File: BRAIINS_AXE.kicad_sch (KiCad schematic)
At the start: 5 parts, among them J9 molex_mini_fit

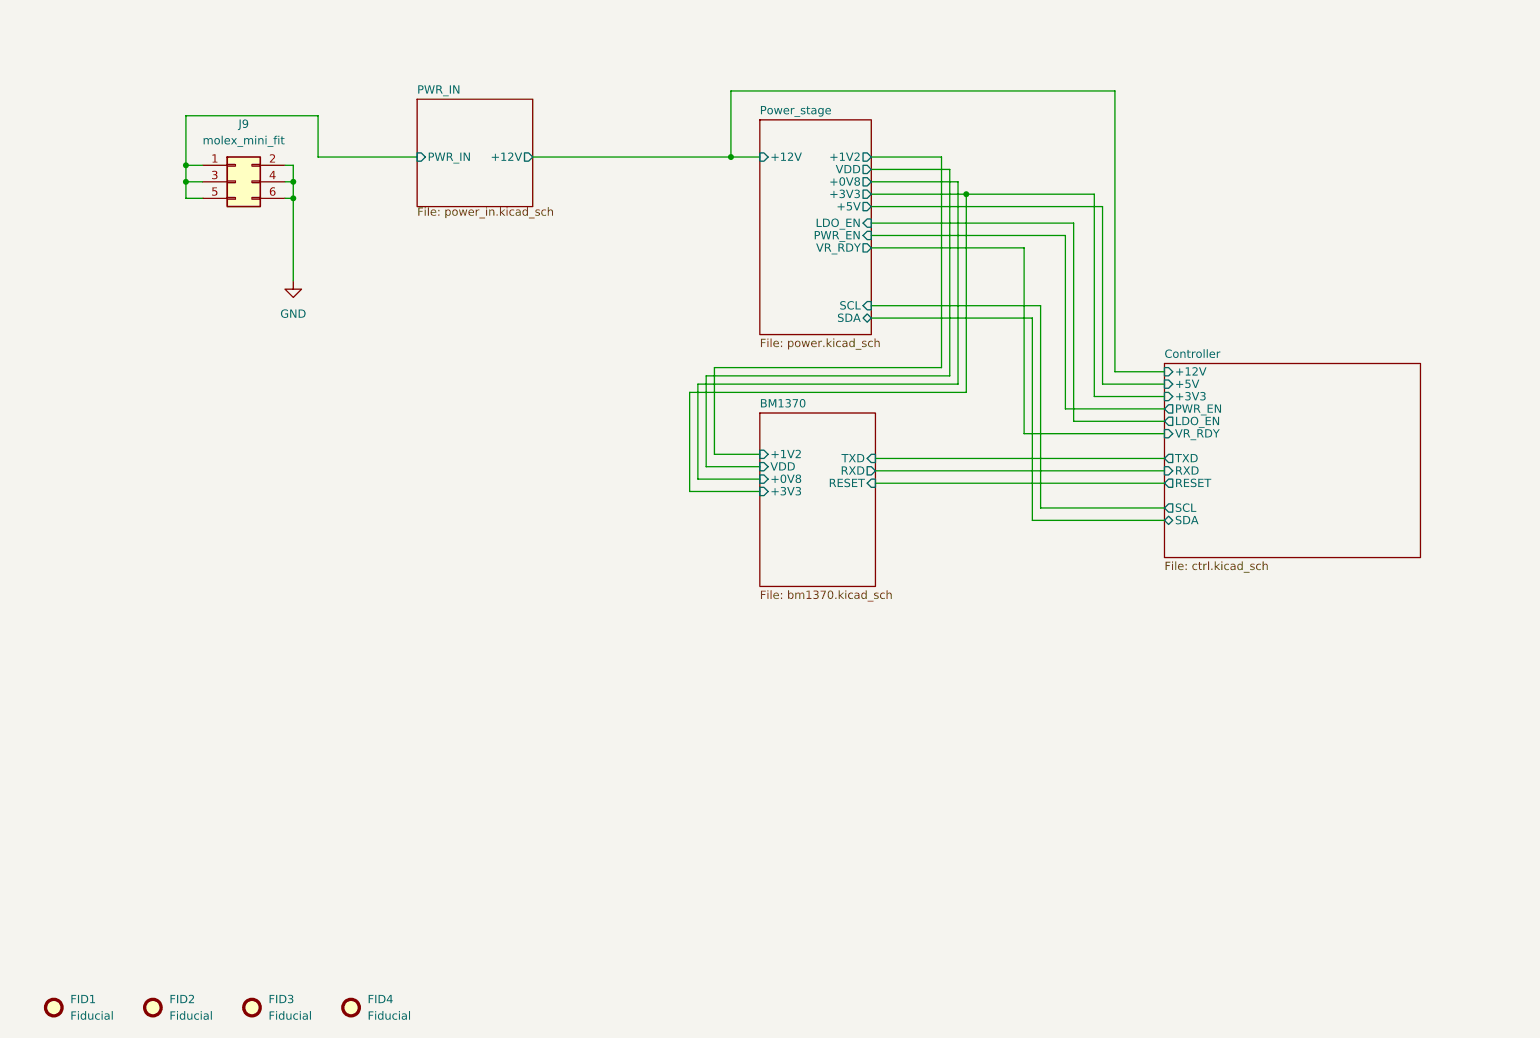
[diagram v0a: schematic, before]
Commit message: updated power stage placements
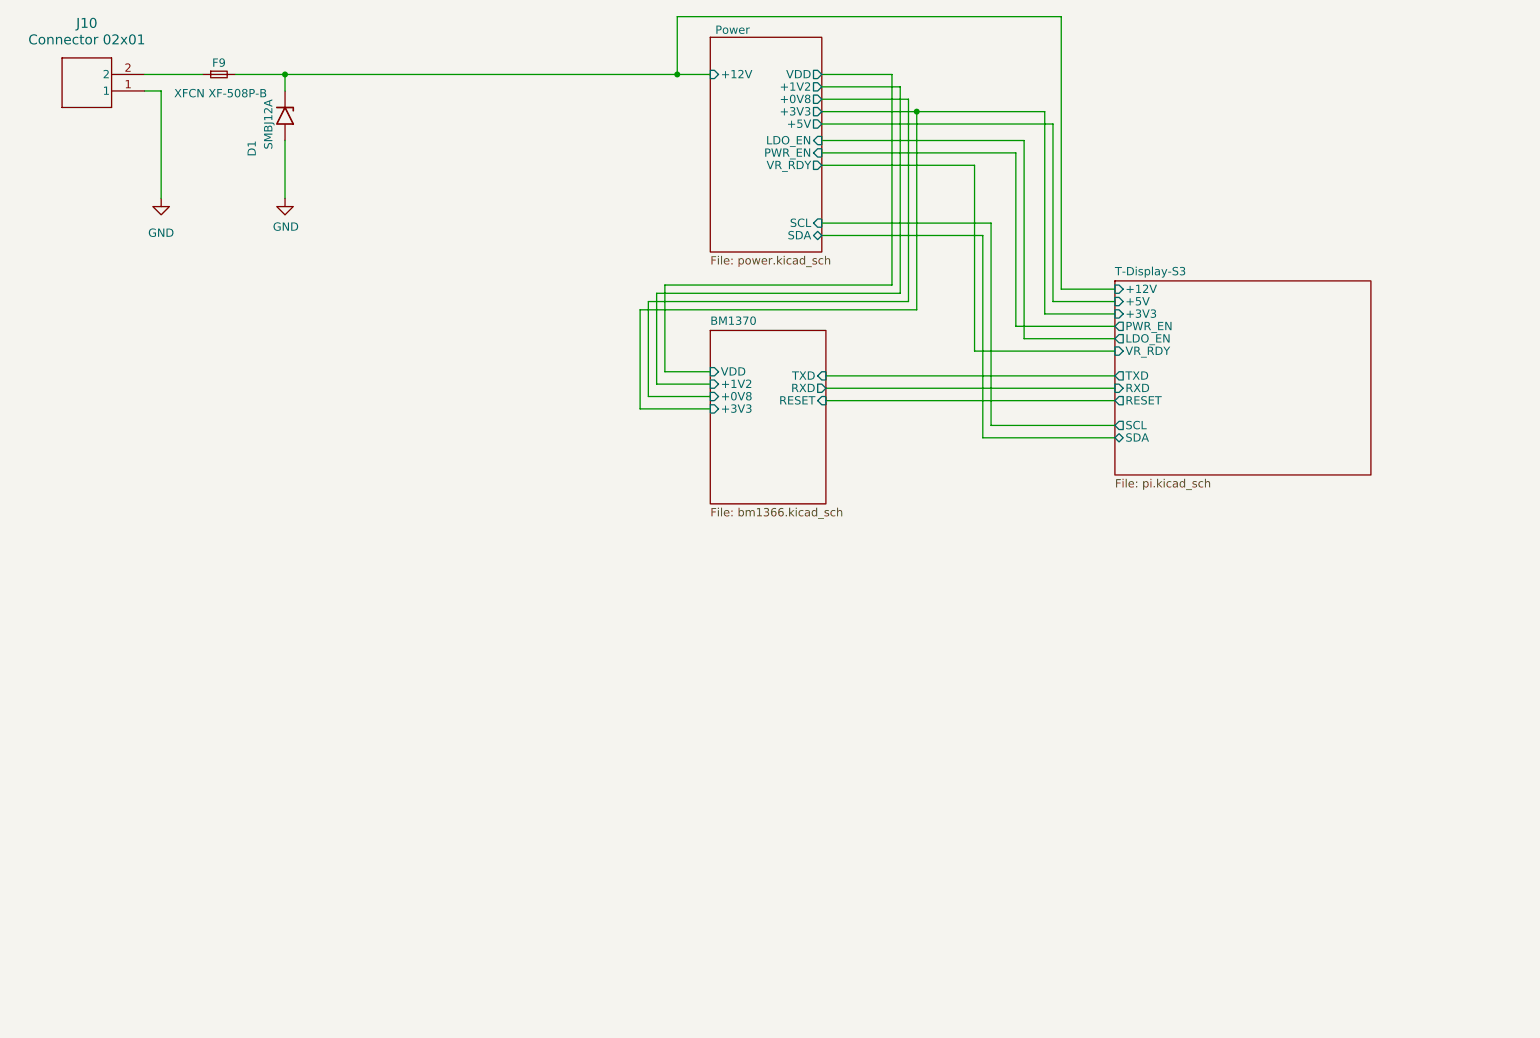
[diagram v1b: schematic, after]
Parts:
- removed FID1, FID2, FID3, FID4: Fiducial, Fiducial:Fiducial_1mm_Mask2mm, symbol Mechanical:Fiducial
- removed J9: molex_mini_fit, Connector_Molex:Molex_Mini-Fit_Jr_5569-06A2_2x03_P4.20mm_Horizontal, symbol Connector_Generic:Conn_02x03_Odd_Even
- added D1: SMBJ12A, Diode_SMD:D_SMB, symbol Diode:5KPxxA
- added F9: XFCN XF-508P-B, Nerd8:XFCN XF-508P-B, symbol Device:Fuse_Small
- added J10: Connector 02x01, Connector_AMASS:AMASS_XT60PW-M_1x02_P7.20mm_Horizontal, symbol CONN02:OSTYK51102030
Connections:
- net GND: now also D1.2 (A2), J10.1
- new net: F9.1, J10.2
- new net Power/+12V: D1.1 (A1), F9.2
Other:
- sheet Controller renamed T-Display-S3
- sheet Power_stage renamed Power
- removed sheet PWR_IN
- sheet BM1370: file bm1370.kicad_sch -> bm1366.kicad_sch
- sheet T-Display-S3: file ctrl.kicad_sch -> pi.kicad_sch

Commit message: power stage in place
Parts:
- added H1, H2: MountingHole, MountingHole:MountingHole_3.2mm_M3_Pad_Via, symbol Mechanical:MountingHole
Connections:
- net Power/+12V: no longer D1.1 (A1)
- net at F9.1, J10.2: now also D1.1 (A1)
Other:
- sheet T-Display-S3 renamed controller
- sheet controller: file pi.kicad_sch -> CONTROL.kicad_sch
- moved on the sheet: D1, F9
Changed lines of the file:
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@@
 	)
 	(junction
-		(at 55.88 52.07)
+		(at 46.99 52.07)
 		(diameter 0)
 		(color 0 0 0 0)
@@
 	(wire
 		(pts
+			(xy 46.99 52.07) (xy 55.88 52.07)
+		)
+		(stroke
+			(width 0)
+			(type default)
+		)
+	)
+	(wire
+		(pts
 			(xy 138.43 76.835) (xy 163.195 76.835)
 		)
@@
 	(wire
 		(pts
-			(xy 34.29 52.07) (xy 43.18 52.07)
+			(xy 34.29 52.07) (xy 46.99 52.07)
 		)
 		(stroke
@@
 	(wire
 		(pts
-			(xy 48.26 52.07) (xy 55.88 52.07)
-		)
-		(stroke
-			(width 0)
-			(type default)
-		)
-	)
-	(wire
-		(pts
 			(xy 149.225 52.07) (xy 149.225 84.455)
 		)
@@
 	(wire
 		(pts
-			(xy 55.88 54.61) (xy 55.88 52.07)
+			(xy 46.99 54.61) (xy 46.99 52.07)
 		)
 		(stroke
@@
 	(wire
 		(pts
+			(xy 60.96 52.07) (xy 116.205 52.07)
+		)
+		(stroke
+			(width 0)
+			(type default)
+		)
+	)
+	(wire
+		(pts
 			(xy 138.43 66.04) (xy 161.925 66.04)
 		)
@@
 	(wire
 		(pts
-			(xy 55.88 62.23) (xy 55.88 71.12)
+			(xy 46.99 62.23) (xy 46.99 71.12)
 		)
 		(stroke
@@
 		(pts
 			(xy 161.925 66.04) (xy 161.925 94.615)
-		)
-		(stroke
-			(width 0)
-			(type default)
-		)
-	)
-	(wire
-		(pts
-			(xy 55.88 52.07) (xy 116.205 52.07)
 		)
 		(stroke
@@
 	(symbol
 		(lib_id "power:GND")
-		(at 55.88 71.12 0)
+		(at 46.99 71.12 0)
 		(unit 1)
 		(body_style 1)
@@
 		(dnp no)
 		(property "Reference" "#PWR04"
-			(at 55.88 77.47 0)
+			(at 46.99 77.47 0)
 			(hide yes)
 			(show_name no)
@@
 		)
 		(property "Value" "GND"
-			(at 56.007 75.5142 0)
+			(at 47.117 75.5142 0)
 			(show_name no)
 			(do_not_autoplace no)
@@
 		)
 		(property "Footprint" ""
-			(at 55.88 71.12 0)
+			(at 46.99 71.12 0)
 			(hide yes)
 			(show_name no)
@@
 		)
 		(property "Datasheet" ""
-			(at 55.88 71.12 0)
+			(at 46.99 71.12 0)
 			(hide yes)
 			(show_name no)
@@
 		)
 		(property "Description" ""
-			(at 55.88 71.12 0)
+			(at 46.99 71.12 0)
 			(hide yes)
 			(show_name no)
@@
 	(symbol
 		(lib_id "Diode:5KPxxA")
-		(at 55.88 58.42 270)
+		(at 46.99 58.42 270)
 		(unit 1)
 		(body_style 1)
@@
 		(dnp no)
 		(property "Reference" "D1"
-			(at 50.8 62.23 0)
+			(at 48.26 61.722 90)
 			(show_name no)
 			(do_not_autoplace no)
@@
 		)
 		(property "Value" "SMBJ12A"
-			(at 53.34 55.88 0)
+			(at 44.45 55.88 0)
 			(show_name no)
 			(do_not_autoplace no)
@@
 		)
 		(property "Footprint" "Diode_SMD:D_SMB"
-			(at 50.8 58.42 0)
+			(at 41.91 58.42 0)
 			(hide yes)
 			(show_name no)
@@
 		)
 		(property "Datasheet" ""
-			(at 55.88 57.15 0)
+			(at 46.99 57.15 0)
 			(hide yes)
 			(show_name no)
@@
 		)
 		(property "Description" "TVS DIODE 12VWM 19.9VC DO214AA"
-			(at 55.88 58.42 0)
+			(at 46.99 58.42 0)
 			(hide yes)
 			(show_name no)
@@
 		)
 		(property "Distributor" "D"
-			(at 55.88 58.42 0)
+			(at 46.99 58.42 0)
 			(hide yes)
 			(show_name no)
@@
 		)
 		(property "Manufacturer" "SMBJ12A"
-			(at 55.88 58.42 0)
+			(at 46.99 58.42 0)
 			(hide yes)
 			(show_name no)
@@
 		)
 		(property "OrderNr" "SMBJ12ALFCT-ND"
-			(at 55.88 58.42 0)
+			(at 46.99 58.42 0)
 			(hide yes)
 			(show_name no)
@@
 	)
 	(symbol
+		(lib_id "Mechanical:MountingHole")
+		(at 165.1 161.29 0)
+		(unit 1)
+		(body_style 1)
+		(exclude_from_sim no)
+		(in_bom no)
+		(on_board yes)
+		(in_pos_files yes)
+		(dnp no)
+		(fields_autoplaced yes)
+		(property "Reference" "H1"
+			(at 167.64 160.0199 0)
+			(show_name no)
+			(do_not_autoplace no)
+			(effects
+				(font
+					(size 1.27 1.27)
+				)
+				(justify left)
+			)
+		)
+		(property "Value" "MountingHole"
+			(at 167.64 162.5599 0)
+			(show_name no)
+			(do_not_autoplace no)
+			(effects
+				(font
+					(size 1.27 1.27)
+				)
+				(justify left)
+			)
+		)
+		(property "Footprint" "MountingHole:MountingHole_3.2mm_M3_Pad_Via"
+			(at 165.1 161.29 0)
+			(hide yes)
+			(show_name no)
+			(do_not_autoplace no)
+			(effects
+				(font
+					(size 1.27 1.27)
+				)
+			)
+		)
+		(property "Datasheet" ""
+			(at 165.1 161.29 0)
+			(hide yes)
+			(show_name no)
+			(do_not_autoplace no)
+			(effects
+				(font
+					(size 1.27 1.27)
+				)
+			)
+		)
+		(property "Description" "Mounting Hole without connection"
+			(at 165.1 161.29 0)
+			(hide yes)
+			(show_name no)
+			(do_not_autoplace no)
+			(effects
+				(font
+					(size 1.27 1.27)
+				)
+			)
+		)
+		(instances
+			(project "BRAIINS_AXE"
+				(path "/e63e39d7-6ac0-4ffd-8aa3-1841a4541b55"
+					(reference "H1")
+					(unit 1)
+				)
+			)
+		)
+	)
+	(symbol
 		(lib_id "CONN02:OSTYK51102030")
 		(at 34.29 54.61 180)
@@
 	)
 	(symbol
+		(lib_id "Mechanical:MountingHole")
+		(at 186.69 161.29 0)
+		(unit 1)
+		(body_style 1)
+		(exclude_from_sim no)
+		(in_bom no)
+		(on_board yes)
+		(in_pos_files yes)
+		(dnp no)
+		(fields_autoplaced yes)
+		(property "Reference" "H2"
+			(at 189.23 160.0199 0)
+			(show_name no)
+			(do_not_autoplace no)
+			(effects
+				(font
+					(size 1.27 1.27)
+				)
+				(justify left)
+			)
+		)
+		(property "Value" "MountingHole"
+			(at 189.23 162.5599 0)
+			(show_name no)
+			(do_not_autoplace no)
+			(effects
+				(font
+					(size 1.27 1.27)
+				)
+				(justify left)
+			)
+		)
+		(property "Footprint" "MountingHole:MountingHole_3.2mm_M3_Pad_Via"
+			(at 186.69 161.29 0)
+			(hide yes)
+			(show_name no)
+			(do_not_autoplace no)
+			(effects
+				(font
+					(size 1.27 1.27)
+				)
+			)
+		)
+		(property "Datasheet" ""
+			(at 186.69 161.29 0)
+			(hide yes)
+			(show_name no)
+			(do_not_autoplace no)
+			(effects
+				(font
+					(size 1.27 1.27)
+				)
+			)
+		)
+		(property "Description" "Mounting Hole without connection"
+			(at 186.69 161.29 0)
+			(hide yes)
+			(show_name no)
+			(do_not_autoplace no)
+			(effects
+				(font
+					(size 1.27 1.27)
+				)
+			)
+		)
+		(instances
+			(project "BRAIINS_AXE"
+				(path "/e63e39d7-6ac0-4ffd-8aa3-1841a4541b55"
+					(reference "H2")
+					(unit 1)
+				)
+			)
+		)
+	)
+	(symbol
 		(lib_id "Device:Fuse_Small")
-		(at 45.72 52.07 0)
+		(at 58.42 52.07 0)
 		(unit 1)
 		(body_style 1)
@@
 		(dnp no)
 		(property "Reference" "F9"
-			(at 45.72 50.292 0)
+			(at 58.42 50.292 0)
 			(show_name no)
 			(do_not_autoplace no)
@@
 		)
 		(property "Value" "XFCN XF-508P-B"
-			(at 45.974 54.991 0)
+			(at 58.674 54.991 0)
 			(show_name no)
 			(do_not_autoplace no)
@@
 		)
 		(property "Footprint" "Nerd8:XFCN XF-508P-B"
-			(at 45.72 52.07 0)
+			(at 58.42 52.07 0)
 			(hide yes)
 			(show_name no)
@@
 		)
 		(property "Datasheet" ""
-			(at 45.72 52.07 0)
+			(at 58.42 52.07 0)
 			(hide yes)
 			(show_name no)
@@
 		)
 		(property "Description" ""
-			(at 45.72 52.07 0)
+			(at 58.42 52.07 0)
 			(show_name no)
 			(do_not_autoplace no)
@@
 		)
 		(property "shop" "https://www.tme.eu/cz/details/keys3568/automobilni-pojistkova-pouzdra/keystone/3568/"
-			(at 45.72 52.07 0)
+			(at 58.42 52.07 0)
 			(hide yes)
 			(show_name no)
@@
 		)
 		(property "LCSC" "C2935468"
-			(at 45.72 52.07 0)
+			(at 58.42 52.07 0)
 			(hide yes)
 			(show_name no)
@@
 			(color 255 255 194 1)
 		)
-		(property "Sheetname" "T-Display-S3"
+		(property "Sheetname" "controller"
 			(at 183.515 83.1084 0)
 			(show_name no)
@@
 			)
 		)
-		(property "Sheetfile" "pi.kicad_sch"
+		(property "Sheetfile" "CONTROL.kicad_sch"
 			(at 183.515 114.2496 0)
 			(show_name no)

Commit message: shrinking layout to fit
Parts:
- added H3, H4, H5, H6: MountingHole, MountingHole:MountingHole_3.2mm_M3_Pad_Via, symbol Mechanical:MountingHole

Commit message: placing W5500
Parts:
- removed F9: XFCN XF-508P-B, Nerd8:XFCN XF-508P-B, symbol Device:Fuse_Small
- added F1: Bourns SF-1206HHA1500R-2, Fuse:Fuse_1210_3225Metric, symbol Device:Fuse_Small
- added H7, H8: MountingHole, MountingHole:MountingHole_3.2mm_M3_Pad_Via, symbol Mechanical:MountingHole
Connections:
- net Power/+12V: now also F1.2
- net at D1.1 (A1), J10.2: now also F1.1
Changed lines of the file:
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@@
+	)
+	(symbol
+		(lib_id "Device:Fuse_Small")
+		(at 58.42 52.07 0)
+		(unit 1)
+		(body_style 1)
+		(exclude_from_sim no)
+		(in_bom yes)
+		(on_board yes)
+		(in_pos_files yes)
+		(dnp no)
+		(fields_autoplaced yes)
+		(property "Reference" "F1"
+			(at 58.42 46.99 0)
+			(show_name no)
+			(do_not_autoplace no)
+			(effects
+				(font
+					(size 1.27 1.27)
+				)
+			)
+		)
+		(property "Value" "Bourns SF-1206HHA1500R-2"
+			(at 58.42 49.53 0)
+			(show_name no)
+			(do_not_autoplace no)
+			(effects
+				(font
+					(size 1.27 1.27)
+				)
+			)
+		)
+		(property "Footprint" "Fuse:Fuse_1210_3225Metric"
+			(at 58.42 52.07 0)
+			(hide yes)
+			(show_name no)
+			(do_not_autoplace no)
+			(effects
+				(font
+					(size 1.27 1.27)
+				)
+			)
+		)
+		(property "Datasheet" ""
+			(at 58.42 52.07 0)
+			(hide yes)
+			(show_name no)
+			(do_not_autoplace no)
+			(effects
+				(font
+					(size 1.27 1.27)
+				)
+			)
+		)
+		(property "Description" "Fuse, small symbol"
+			(at 58.42 52.07 0)
+			(hide yes)
+			(show_name no)
+			(do_not_autoplace no)
+			(effects
+				(font
+					(size 1.27 1.27)
+				)
+			)
+		)
+		(pin "1"
+		)
+		(pin "2"
+		)
+		(instances
+			(project "BRAIINS_AXE"
+				(path "/e63e39d7-6ac0-4ffd-8aa3-1841a4541b55"
+					(reference "F1")
+					(unit 1)
+				)
+			)
+		)
 	)
 	(symbol
@@
 	(symbol
 		(lib_id "Mechanical:MountingHole")
+		(at 208.28 144.78 0)
+		(unit 1)
+		(body_style 1)
+		(exclude_from_sim no)
+		(in_bom no)
+		(on_board yes)
+		(in_pos_files yes)
+		(dnp no)
+		(fields_autoplaced yes)
+		(property "Reference" "H7"
+			(at 210.82 143.5099 0)
+			(show_name no)
+			(do_not_autoplace no)
+			(effects
+				(font
+					(size 1.27 1.27)
+				)
+				(justify left)
+			)
+		)
+		(property "Value" "MountingHole"
+			(at 210.82 146.0499 0)
+			(show_name no)
+			(do_not_autoplace no)
+			(effects
+				(font
+					(size 1.27 1.27)
+				)
+				(justify left)
+			)
+		)
+		(property "Footprint" "MountingHole:MountingHole_3.2mm_M3_Pad_Via"
+			(at 208.28 144.78 0)
+			(hide yes)
+			(show_name no)
+			(do_not_autoplace no)
+			(effects
+				(font
+					(size 1.27 1.27)
+				)
+			)
+		)
+		(property "Datasheet" ""
+			(at 208.28 144.78 0)
+			(hide yes)
+			(show_name no)
+			(do_not_autoplace no)
+			(effects
+				(font
+					(size 1.27 1.27)
+				)
+			)
+		)
+		(property "Description" "Mounting Hole without connection"
+			(at 208.28 144.78 0)
+			(hide yes)
+			(show_name no)
+			(do_not_autoplace no)
+			(effects
+				(font
+					(size 1.27 1.27)
+				)
+			)
+		)
+		(instances
+			(project "BRAIINS_AXE"
+				(path "/e63e39d7-6ac0-4ffd-8aa3-1841a4541b55"
+					(reference "H7")
+					(unit 1)
+				)
+			)
+		)
+	)
+	(symbol
+		(lib_id "Mechanical:MountingHole")
 		(at 165.1 144.78 0)
 		(unit 1)
@@
 	(symbol
 		(lib_id "Mechanical:MountingHole")
+		(at 208.28 152.4 0)
+		(unit 1)
+		(body_style 1)
+		(exclude_from_sim no)
+		(in_bom no)
+		(on_board yes)
+		(in_pos_files yes)
+		(dnp no)
+		(fields_autoplaced yes)
+		(property "Reference" "H8"
+			(at 210.82 151.1299 0)
+			(show_name no)
+			(do_not_autoplace no)
+			(effects
+				(font
+					(size 1.27 1.27)
+				)
+				(justify left)
+			)
+		)
+		(property "Value" "MountingHole"
+			(at 210.82 153.6699 0)
+			(show_name no)
+			(do_not_autoplace no)
+			(effects
+				(font
+					(size 1.27 1.27)
+				)
+				(justify left)
+			)
+		)
+		(property "Footprint" "MountingHole:MountingHole_3.2mm_M3_Pad_Via"
+			(at 208.28 152.4 0)
+			(hide yes)
+			(show_name no)
+			(do_not_autoplace no)
+			(effects
+				(font
+					(size 1.27 1.27)
+				)
+			)
+		)
+		(property "Datasheet" ""
+			(at 208.28 152.4 0)
+			(hide yes)
+			(show_name no)
+			(do_not_autoplace no)
+			(effects
+				(font
+					(size 1.27 1.27)
+				)
+			)
+		)
+		(property "Description" "Mounting Hole without connection"
+			(at 208.28 152.4 0)
+			(hide yes)
+			(show_name no)
+			(do_not_autoplace no)
+			(effects
+				(font
+					(size 1.27 1.27)
+				)
+			)
+		)
+		(instances
+			(project "BRAIINS_AXE"
+				(path "/e63e39d7-6ac0-4ffd-8aa3-1841a4541b55"
+					(reference "H8")
+					(unit 1)
+				)
+			)
+		)
+	)
+	(symbol
+		(lib_id "Mechanical:MountingHole")
 		(at 165.1 152.4 0)
 		(unit 1)
@@
 					(unit 1)
 				)
-			)
-		)
-	)
-	(symbol
-		(lib_id "Device:Fuse_Small")
-		(at 58.42 52.07 0)
-		(unit 1)
-		(body_style 1)
-		(exclude_from_sim no)
-		(in_bom yes)
-		(on_board yes)
-		(in_pos_files yes)
-		(dnp no)
-		(property "Reference" "F9"
-			(at 58.42 50.292 0)
-			(show_name no)
-			(do_not_autoplace no)
-			(effects
-				(font
-					(size 1.27 1.27)
-				)
-			)
-		)
-		(property "Value" "XFCN XF-508P-B"
-			(at 58.674 54.991 0)
-			(show_name no)
-			(do_not_autoplace no)
-			(effects
-				(font
-					(size 1.27 1.27)
-				)
-			)
-		)
-		(property "Footprint" "Nerd8:XFCN XF-508P-B"
-			(at 58.42 52.07 0)
-			(hide yes)
-			(show_name no)
-			(do_not_autoplace no)
-			(effects
-				(font
-					(size 1.27 1.27)
-				)
-			)
-		)
-		(property "Datasheet" ""
-			(at 58.42 52.07 0)
-			(hide yes)
-			(show_name no)
-			(do_not_autoplace no)
-			(effects
-				(font
-					(size 1.27 1.27)
-				)
-			)
-		)
-		(property "Description" ""
-			(at 58.42 52.07 0)
-			(show_name no)
-			(do_not_autoplace no)
-			(effects
-				(font
-					(size 1.27 1.27)
-				)
-			)
-		)
-		(property "shop" "https://www.tme.eu/cz/details/keys3568/automobilni-pojistkova-pouzdra/keystone/3568/"
-			(at 58.42 52.07 0)
-			(hide yes)
-			(show_name no)
-			(do_not_autoplace no)
-			(effects
-				(font
-					(size 1.27 1.27)
-				)
-			)
-		)
-		(property "LCSC" "C2935468"
-			(at 58.42 52.07 0)
-			(hide yes)
-			(show_name no)
-			(do_not_autoplace no)
-			(effects
-				(font
-					(size 1.27 1.27)
-				)
-			)
-		)
-		(pin "1"
-		)
-		(pin "2"
-		)
-		(instances
-			(project "BRAIINS_AXE"
-				(path "/e63e39d7-6ac0-4ffd-8aa3-1841a4541b55"
-					(reference "F9")
-					(unit 1)
-				)
